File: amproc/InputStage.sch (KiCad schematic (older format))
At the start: 19 parts, among them J5 LEFT IN, J6 RIGHT IN, U1 TL072, U2 TL072

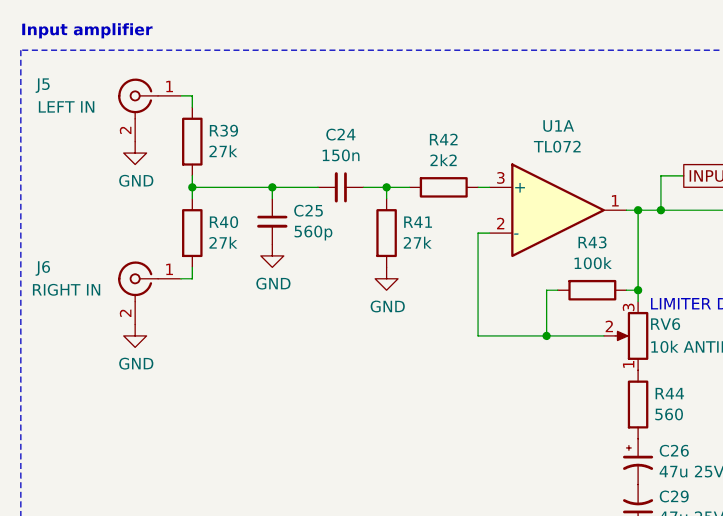
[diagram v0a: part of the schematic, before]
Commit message: Change C25 to 100pF to reduce high frequency attenuation
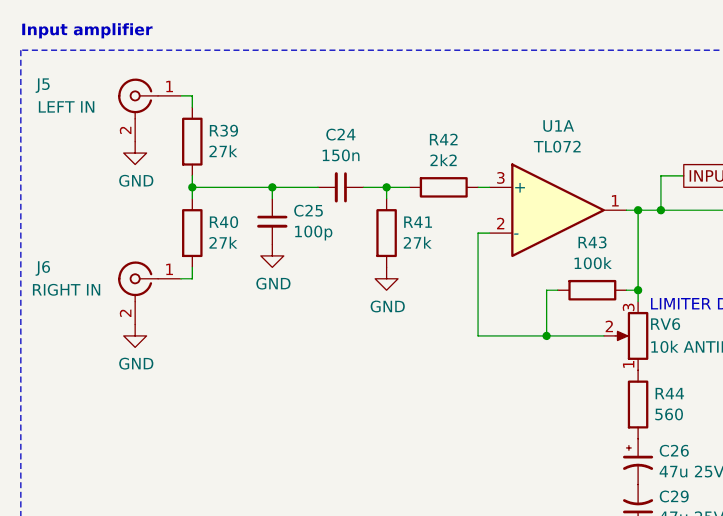
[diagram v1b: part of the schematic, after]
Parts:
- C25: value 560p -> 100p
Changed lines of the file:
@@
 P 3950 3000
 F 0 "C25" H 4042 3046 50  0000 L CNN
-F 1 "560p" H 4042 2955 50  0000 L CNN
+F 1 "100p" H 4042 2955 50  0000 L CNN
 F 2 "Capacitors_THT:C_Disc_D5.0mm_W2.5mm_P2.50mm" H 3950 3000 50  0001 C CNN
 F 3 "~" H 3950 3000 50  0001 C CNN

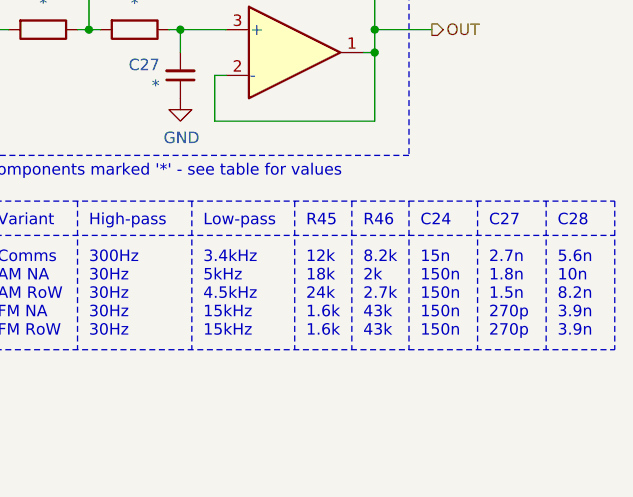
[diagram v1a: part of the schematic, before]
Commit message: Changed LPF, pre-emphasis component values in AM (NA and RoW) variants to correct bandwidth
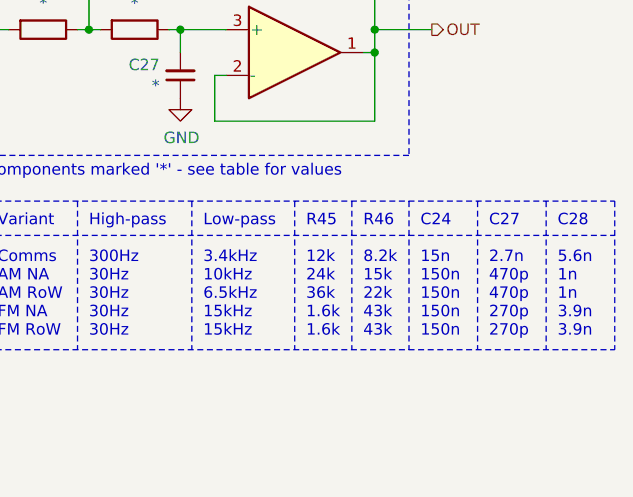
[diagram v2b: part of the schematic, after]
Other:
- note added: "C27\n\n2.7n\n470p\n470p\n270p\n270p"
- note added: "C28\n\n5.6n\n1n\n1n\n3.9n\n3.9n"
- note added: "Low-pass\n\n3.4kHz\n10kHz\n6.5kHz\n15kHz\n15kHz"
- note added: "R45\n\n12k\n24k\n36k\n1.6k\n1.6k"
- note added: "R46\n\n8.2k\n15k\n22k\n43k\n43k"
- note removed: "C27\n\n2.7n\n1.8n\n1.5n\n270p\n270p"
- note removed: "C28\n\n5.6n\n10n\n8.2n\n3.9n\n3.9n"
- note removed: "Low-pass\n\n3.4kHz\n5kHz\n4.5kHz\n15kHz\n15kHz"
- note removed: "R45\n\n12k\n18k\n24k\n1.6k\n1.6k"
- note removed: "R46\n\n8.2k\n2k\n2.7k\n43k\n43k"
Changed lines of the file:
@@
 	5650 2950 6500 2950
 Text Notes 7350 4300 0    50   ~ 0
-Low-pass\n\n3.4kHz\n5kHz\n4.5kHz\n15kHz\n15kHz
+Low-pass\n\n3.4kHz\n10kHz\n6.5kHz\n15kHz\n15kHz
 Text Notes 6850 4300 0    50   ~ 0
 High-pass\n\n300Hz\n30Hz\n30Hz\n30Hz\n30Hz
@@
 C24\n\n15n\n150n\n150n\n150n\n150n
 Text Notes 7800 4300 0    50   ~ 0
-R45\n\n12k\n18k\n24k\n1.6k\n1.6k
+R45\n\n12k\n24k\n36k\n1.6k\n1.6k
 Text Notes 8050 4300 0    50   ~ 0
-R46\n\n8.2k\n2k\n2.7k\n43k\n43k
+R46\n\n8.2k\n15k\n22k\n43k\n43k
 Text Notes 8600 4300 0    50   ~ 0
-C27\n\n2.7n\n1.8n\n1.5n\n270p\n270p
+C27\n\n2.7n\n470p\n470p\n270p\n270p
 Text Notes 8900 4300 0    50   ~ 0
-C28\n\n5.6n\n10n\n8.2n\n3.9n\n3.9n
+C28\n\n5.6n\n1n\n1n\n3.9n\n3.9n
 Wire Notes Line style solid
 	9150 3700 9150 4350
